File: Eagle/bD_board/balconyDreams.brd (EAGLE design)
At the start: 100 x 80 mm, 19 parts, among them IC1 7805L, U1 MKR1000, X2 MKDSN1,5/2-5,08

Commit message: add 2n7001 mosfets for relais outputs
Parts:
- added Q4: 2N7002, transistors_gaui:SOT23
- added R8: (no value), rcl:R0805
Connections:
- new net RELAIS_1_OUT: Q4.3, SV1.2
- net GND: now also Q4.2
- net RELAIS_1: now also Q4.1, R8.1; no longer SV1.2
- net VCC: now also R8.2
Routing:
- net RELAIS_1: track 29.9 -> 1.93 mm

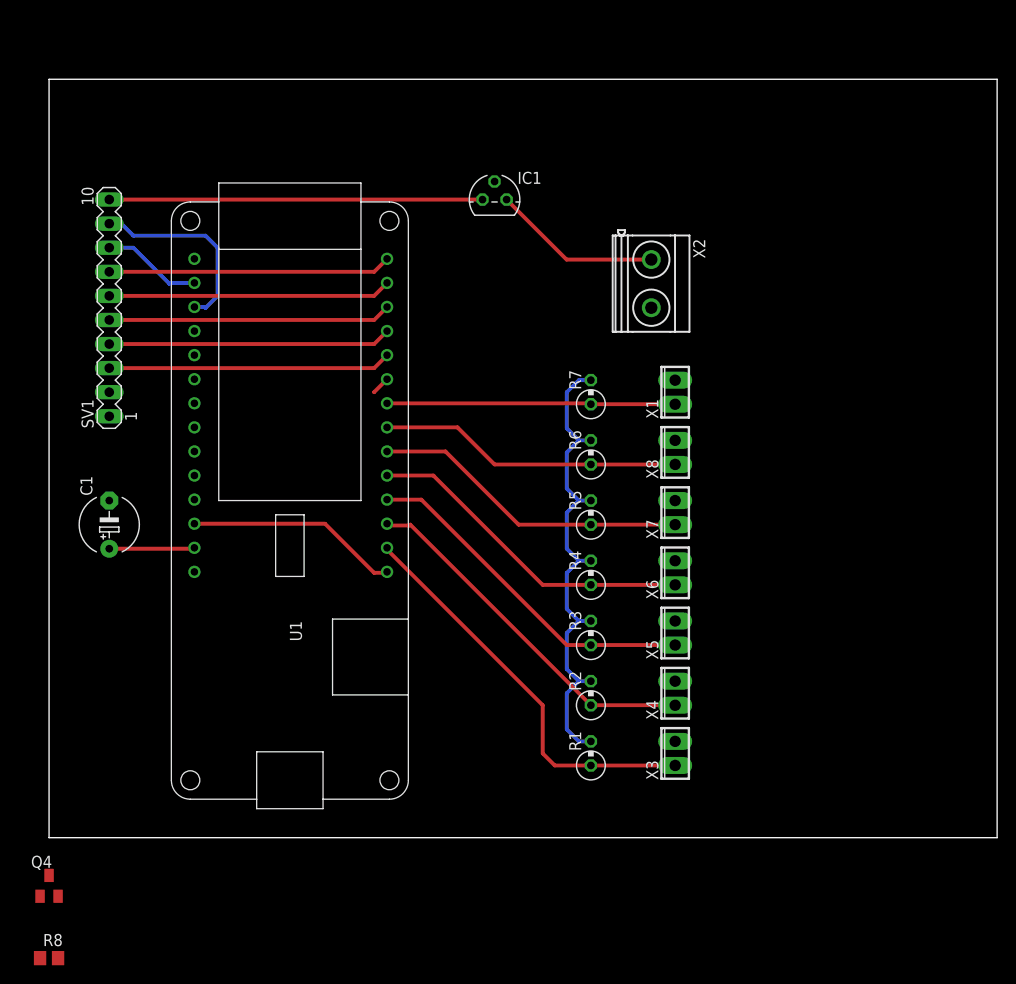
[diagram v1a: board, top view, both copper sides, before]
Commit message: add mosfets for all relais outputs
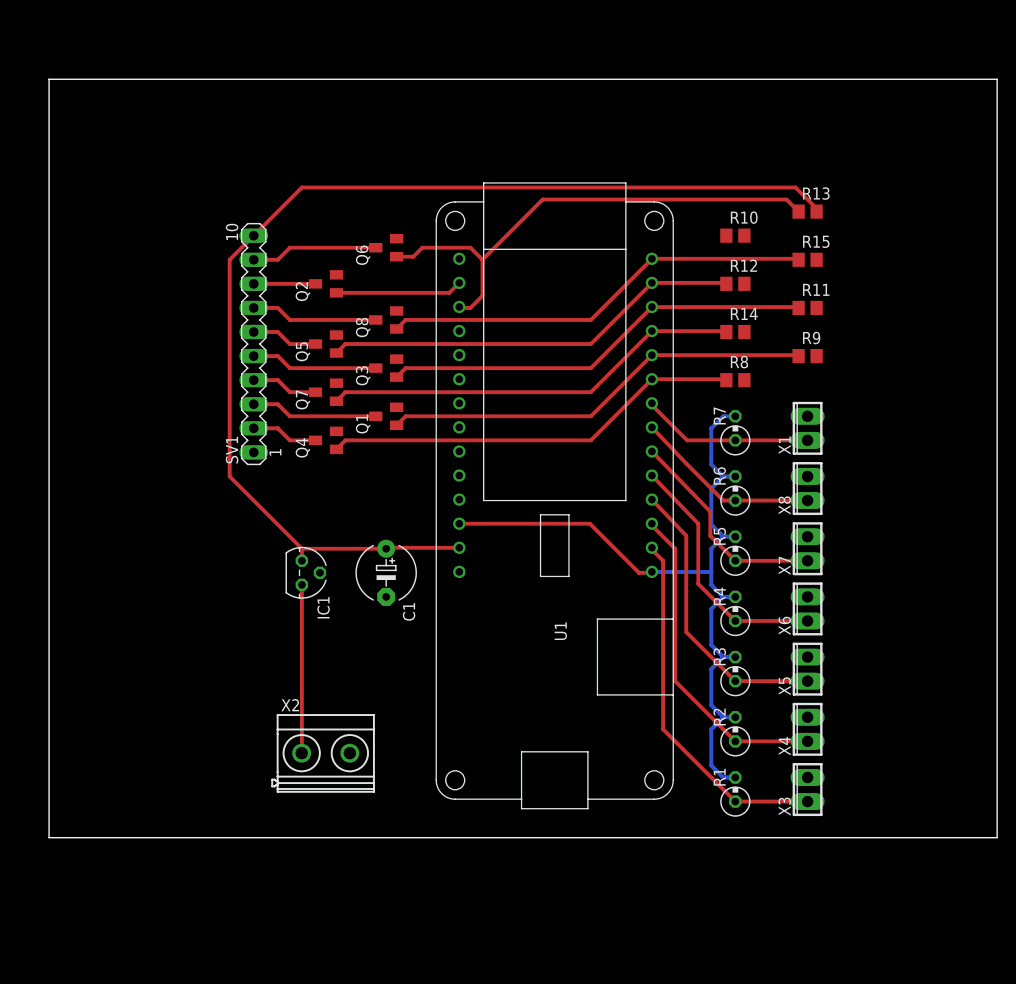
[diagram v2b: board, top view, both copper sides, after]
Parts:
- added Q1, Q2, Q3, Q5, Q6, Q7, Q8: 2N7002, transistors_gaui:SOT23
- added R10, R11, R12, R13, R14, R15, R9: (no value), rcl:R0805
- moved R8 94.6 mm to (72.4, 48.3)
- moved X2 60.2 mm to (29.2, 8.89), turned to 0 degrees
- moved Q4 55.3 mm to (29.2, 41.9), turned to 90 degrees
- moved IC1 44.3 mm to (26.7, 27.9), turned to 270 degrees
- moved C1 29.6 mm to (35.6, 27.9), turned to 270 degrees
- moved U1 27.9 mm to (53.3, 35.6)
- moved R1 15.7 mm to (72.4, 5.08)
- moved R2 15.7 mm to (72.4, 11.4)
- moved R3 15.7 mm to (72.4, 17.8)
- moved R4 15.7 mm to (72.4, 24.1)
- moved R5 15.7 mm to (72.4, 30.5)
- moved R6 15.7 mm to (72.4, 36.8)
- moved R7 15.7 mm to (72.4, 43.2)
- moved SV1 15.7 mm to (21.6, 52.1)
- moved X1 14.5 mm to (80.0, 43.2)
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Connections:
- new net RELAIS_2_OUT: Q1.3, SV1.3
- new net RELAIS_3_OUT: Q7.3, SV1.4
- new net RELAIS_4_OUT: Q3.3, SV1.5
- new net RELAIS_5_OUT: Q5.3, SV1.6
- new net RELAIS_6_OUT: Q8.3, SV1.7
- new net RELAIS_7_OUT: Q2.3, SV1.8
- new net RELAIS_8_OUT: Q6.3, SV1.9
- net GND: now also Q1.2, Q2.2, Q3.2, Q5.2, Q6.2, Q7.2, Q8.2
- net RELAIS_2: now also Q1.1, R9.1; no longer SV1.3
- net RELAIS_3: now also Q7.1, R14.1; no longer SV1.4
- net RELAIS_4: now also Q3.1, R11.1; no longer SV1.5
- net RELAIS_5: now also Q5.1, R12.1; no longer SV1.6
- net RELAIS_6: now also Q8.1, R15.1; no longer SV1.7
- net RELAIS_7: now also Q2.1, R10.1; no longer SV1.8
- net RELAIS_8: now also Q6.1, R13.1; no longer SV1.9
- net VCC: now also R10.2, R11.2, R12.2, R13.2, R14.2, R15.2, R9.2
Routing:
- net VCC: track 48.4 -> 117.9 mm
- net RELAIS_1: track 1.93 -> 44.2 mm
- net RELAIS_8: track 20.6 -> 53.3 mm
- net RELAIS_2: track 29.9 -> 45.5 mm
- net RELAIS_6: track 29.9 -> 45.5 mm
- net RELAIS_4: track 29.9 -> 45.5 mm
- net RELAIS_5: track 29.9 -> 44.2 mm
- net RELAIS_3: track 29.9 -> 44.2 mm
- net RELAIS_6_OUT: track 0.00 -> 13.4 mm
- net RELAIS_8_OUT: track 0.00 -> 13.4 mm
- net RELAIS_4_OUT: track 0.00 -> 13.4 mm
- net RELAIS_2_OUT: track 0.00 -> 13.4 mm
- net A5: track 32.0 -> 19.7 mm
- net A6: track 30.4 -> 18.2 mm
- net A4: track 33.6 -> 22.7 mm
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
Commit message: wired resistors replaced by SMD
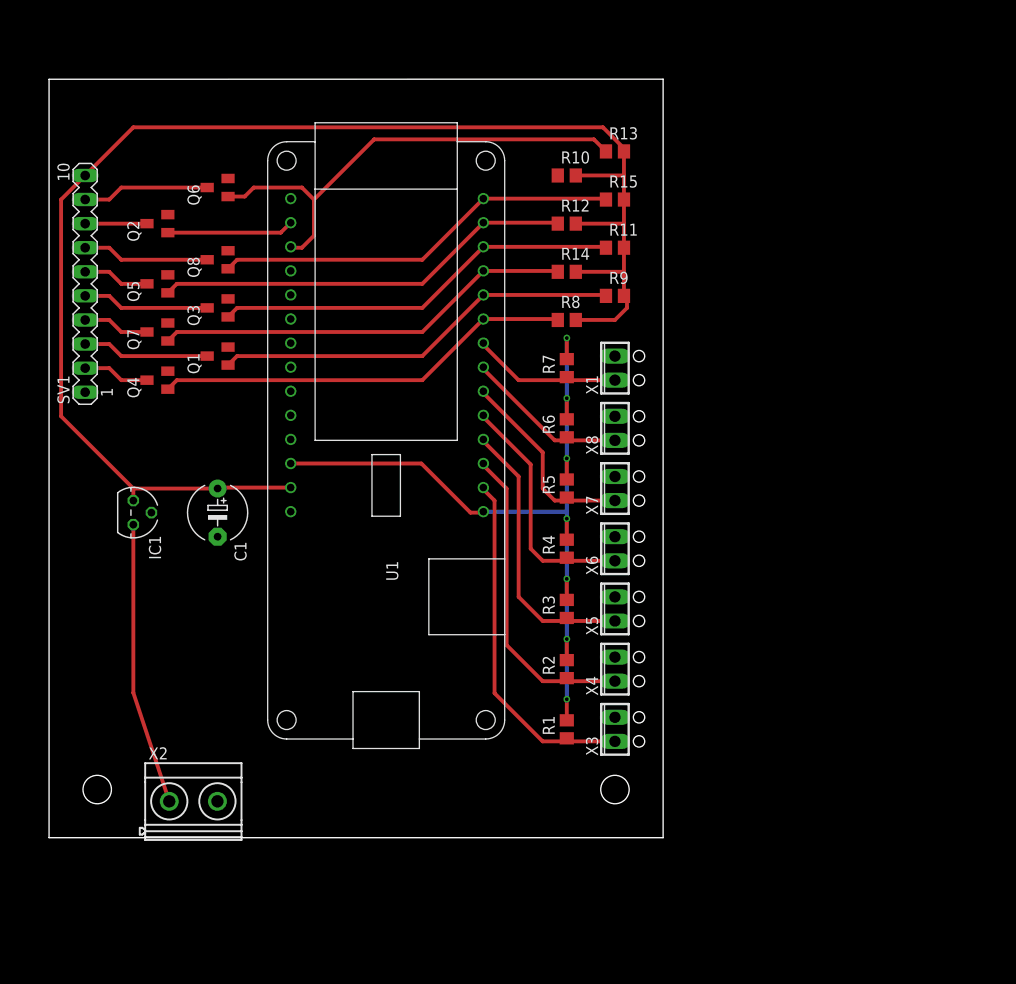
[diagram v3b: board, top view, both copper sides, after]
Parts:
- R1, R2, R3, R4, R5, R6, R7: device rcl:0309V -> rcl:R0805
- moved R15 21.3 mm to (59.7, 67.3)
- moved R9 21.3 mm to (59.7, 57.1)
- moved X1 21.3 mm to (59.7, 49.5)
- moved X3 21.3 mm to (59.7, 11.4)
- moved X4 21.3 mm to (59.7, 17.8)
- moved X6 21.3 mm to (59.7, 30.5)
- moved X8 21.3 mm to (59.7, 43.2)
- moved R11 21.3 mm to (59.7, 62.2)
- moved R13 21.3 mm to (59.7, 72.4)
- moved X5 21.3 mm to (59.7, 24.1)
- moved X7 21.3 mm to (59.7, 36.8)
- moved C1 18.9 mm to (17.8, 34.3)
- moved IC1 18.9 mm to (8.89, 34.3)
- moved Q1 18.9 mm to (17.8, 50.8)
- moved Q2 18.9 mm to (11.4, 64.8)
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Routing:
- net VCC: track 117.9 -> 153.1 mm
- net V_INPUT: track 17.8 -> 29.8 mm
- net +3V3: track 82.1 -> 85.5 mm, vias 0 -> 7
- net RELAIS_6: track 45.5 -> 43.0 mm
- net RELAIS_4: track 45.5 -> 43.0 mm
- net RELAIS_2: track 45.5 -> 43.0 mm
- net RELAIS_8: track 53.3 -> 50.8 mm
- net A6: track 18.2 -> 15.9 mm
- net A5: track 19.7 -> 17.6 mm
- net A4: track 22.7 -> 21.3 mm
- net A1: track 34.2 -> 33.4 mm
- net A0: track 38.0 -> 37.2 mm
- net A2: track 30.4 -> 29.6 mm
- net A3: track 26.6 -> 25.8 mm
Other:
- board size 100 x 80 mm -> 64.8 x 80 mm

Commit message: Lots of stuff - ready for review
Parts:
- added C2: 0.33uF, rcl:E5-6
- added D1, D2, D3, D4, D5, D6, D7: (no value), diode:SOD323-W
- added LED1, LED2, LED3: (no value), led:CHIPLED_0805
- added Q10, Q11, Q9: 2N7002, transistors_gaui:SOT23
- added R16, R18, R20: 10k, rcl:R0805
- added R17, R19, R21: 330R, rcl:R0805
- C1: value (none) -> 1uF
- IC1: value 7805L -> 7805TV; device linear:TO92 -> linear:TO220V
- R10, R11, R12, R13, R14, R15, R8, R9: value (none) -> 10k
- moved IC1 20.1 mm to (15.2, 15.2), turned to 0 degrees
- moved R11 6.35 mm to (53.3, 62.2)
- moved R13 6.35 mm to (53.3, 72.4)
- moved R15 6.35 mm to (53.3, 67.3)
- moved R9 6.35 mm to (53.3, 57.1)
- moved C1 5.12 mm to (17.1, 39.4), turned to 90 degrees
- moved R10 5.08 mm to (59.7, 69.8)
- moved R12 5.08 mm to (59.7, 64.8)
- moved R14 5.08 mm to (59.7, 59.7)
- moved R8 5.08 mm to (59.7, 54.6)
- moved X1 2.54 mm to (62.2, 49.5)
- moved X3 2.54 mm to (62.2, 11.4)
- moved X4 2.54 mm to (62.2, 17.8)
- moved X5 2.54 mm to (62.2, 24.1)
- moved X6 2.54 mm to (62.2, 30.5)
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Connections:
- new net LED1: Q9.1, R16.1, U1.18
- new net LED2: Q10.1, R18.1, U1.19
- new net LED3: Q11.1, R20.1, U1.20
- new net N$1: LED1.C, R17.1
- new net N$2: Q9.3, R17.2
- new net N$3: Q10.3, R19.2
- new net N$4: LED2.C, R19.1
- new net N$5: Q11.3, R21.2
- new net N$6: LED3.C, R21.1
- net A0: now also D1.C
- net A1: now also D2.C
- net A2: now also D3.C
- net A3: now also D4.C
- net A4: now also D5.C
- net A5: now also D6.C
- net A6: now also D7.C
- net GND: now also C2.-, D1.A, D2.A, D3.A, D4.A, D5.A, D6.A, D7.A, Q10.2, Q11.2, Q9.2, R16.2, R18.2, R20.2
- net VCC: now also IC1.3, LED1.A, LED2.A, LED3.A; no longer IC1.1
- net V_INPUT: now also C2.+, IC1.1; no longer IC1.3
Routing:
- net LED1: track 0.00 -> 56.3 mm, vias 0 -> 1
- net VCC: track 153.1 -> 201.7 mm
- net LED2: track 0.00 -> 47.4 mm, vias 0 -> 1
- net LED3: track 0.00 -> 38.0 mm, vias 0 -> 1
- net RELAIS_7: track 13.4 -> 49.4 mm, vias 0 -> 1
- net V_INPUT: track 29.8 -> 14.0 mm
- net RELAIS_8: track 50.8 -> 45.0 mm
- net RELAIS_6: track 43.0 -> 37.3 mm
- net RELAIS_2: track 43.0 -> 37.3 mm
- net RELAIS_1: track 44.2 -> 50.0 mm
- net RELAIS_3: track 44.2 -> 49.9 mm
- net RELAIS_5: track 44.2 -> 49.9 mm
- net RELAIS_4: track 43.0 -> 37.3 mm
- net A1: track 33.4 -> 37.4 mm
- net A6: track 15.9 -> 19.8 mm
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- added copper zone on layer 1, net GND
- added copper zone on layer 16, net GND
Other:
- board size 64.8 x 80 mm -> 67.3 x 80 mm
- board text added: "7-30V"
- board text added: "April 2017"
- board text added: "Balcony Dreams forever"

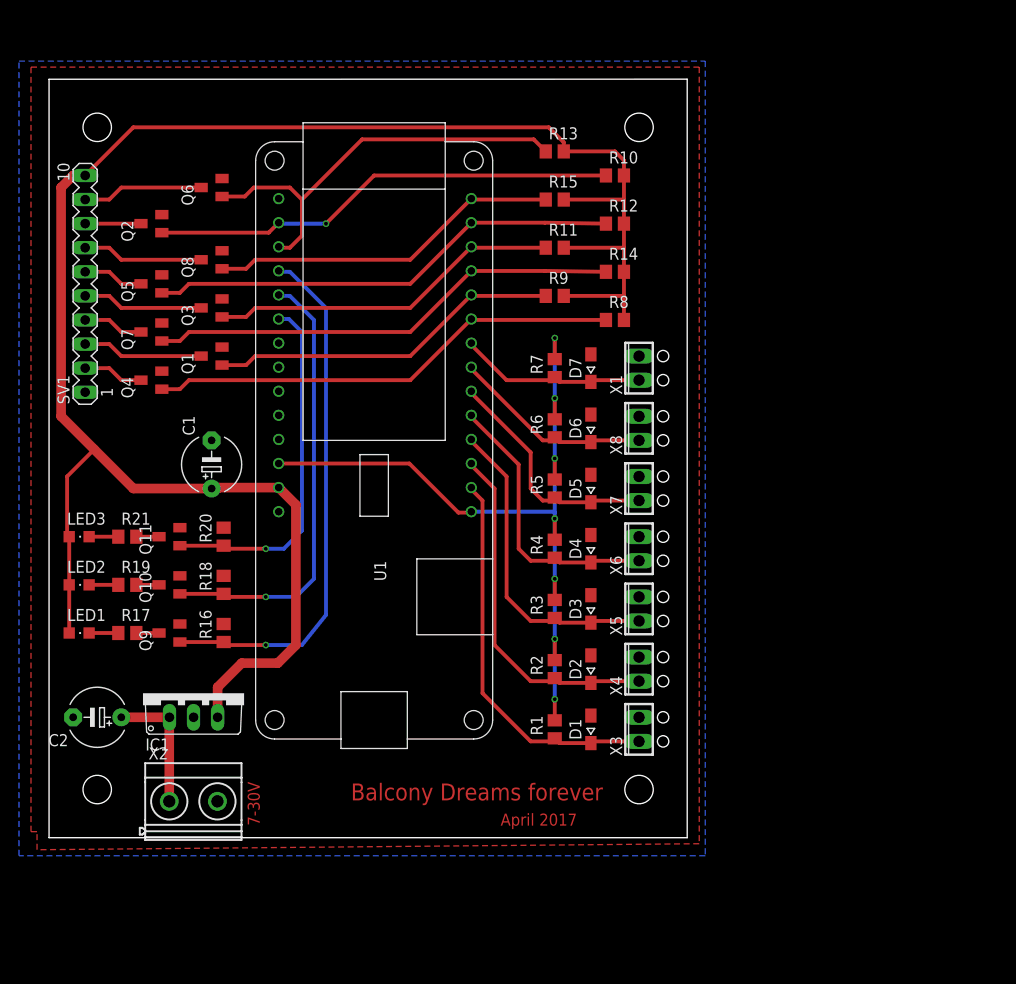
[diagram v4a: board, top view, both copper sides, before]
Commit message: add GND connectors for valves
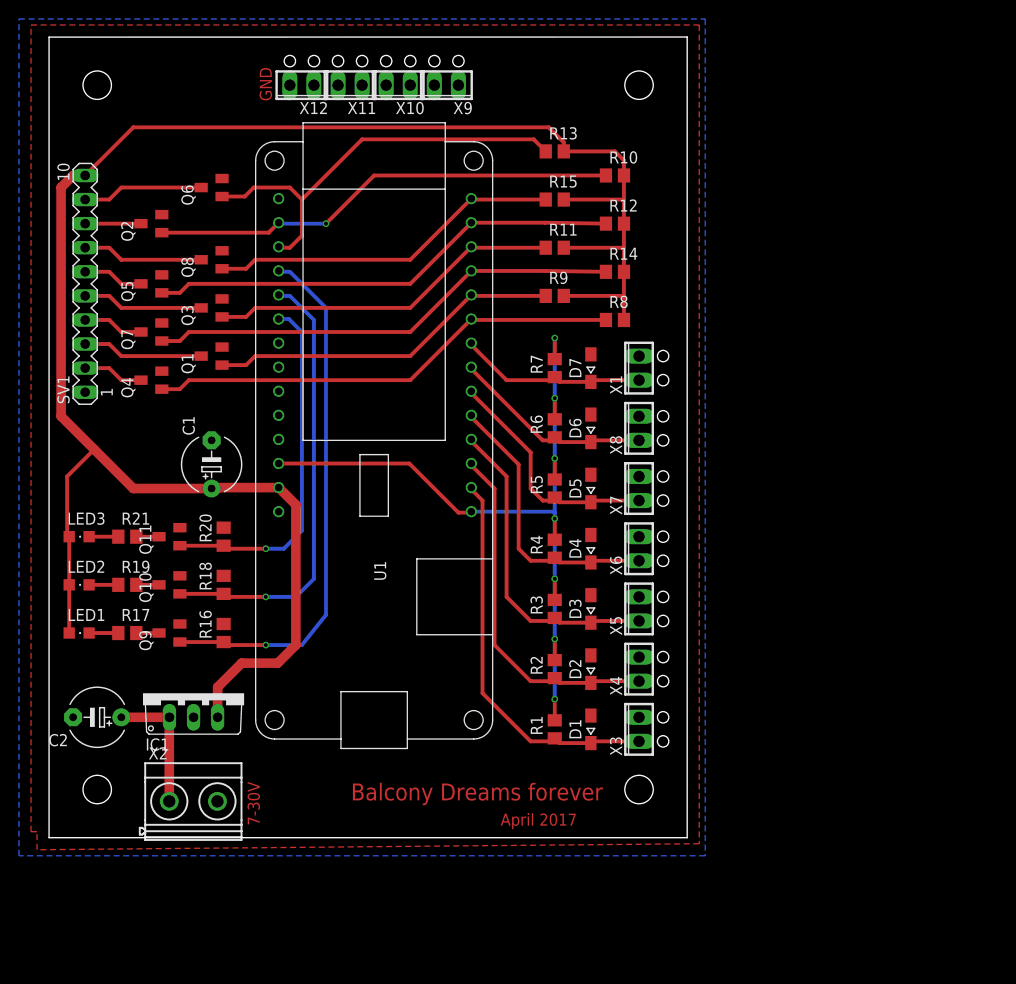
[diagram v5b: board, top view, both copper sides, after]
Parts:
- added X10, X11, X12, X9: (no value), con-phoenix-254:2POL254
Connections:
- net GND: now also X10.1, X10.2, X11.1, X11.2, X12.1, X12.2, X9.1, X9.2
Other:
- board size 67.3 x 80 mm -> 67.3 x 84.5 mm
- board text added: "GND"
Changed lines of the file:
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@@
 <plain>
 <wire x1="0" y1="0" x2="67.31" y2="0" width="0" layer="20"/>
-<wire x1="67.31" y1="0" x2="67.31" y2="80.01" width="0" layer="20"/>
-<wire x1="67.31" y1="80.01" x2="0" y2="80" width="0" layer="20"/>
-<wire x1="0" y1="80" x2="0" y2="0" width="0" layer="20"/>
+<wire x1="67.31" y1="0" x2="67.31" y2="84.455" width="0" layer="20"/>
+<wire x1="67.31" y1="84.455" x2="0" y2="84.445" width="0" layer="20"/>
+<wire x1="0" y1="84.445" x2="0" y2="0" width="0" layer="20"/>
 <hole x="64.77" y="10.16" drill="1.2"/>
 <hole x="64.77" y="12.7" drill="1.2"/>
@@
 <hole x="62.23" y="5.08" drill="3"/>
 <text x="58.42" y="5.715" size="1.778" layer="1" font="vector" ratio="12" rot="R180">Balcony Dreams forever</text>
-<hole x="5.08" y="74.93" drill="3"/>
-<hole x="62.23" y="74.93" drill="3"/>
+<hole x="5.08" y="79.375" drill="3"/>
+<hole x="62.23" y="79.375" drill="3"/>
 <text x="47.625" y="1.27" size="1.27" layer="1" font="vector" ratio="12">April 2017</text>
 <text x="22.225" y="1.27" size="1.27" layer="1" font="vector" ratio="12" rot="R90">7-30V</text>
+<hole x="43.18" y="81.915" drill="1.2"/>
+<hole x="40.64" y="81.915" drill="1.2"/>
+<hole x="38.1" y="81.915" drill="1.2"/>
+<hole x="35.56" y="81.915" drill="1.2"/>
+<hole x="33.02" y="81.915" drill="1.2"/>
+<hole x="30.48" y="81.915" drill="1.2"/>
+<hole x="27.94" y="81.915" drill="1.2"/>
+<hole x="25.4" y="81.915" drill="1.2"/>
+<text x="22.225" y="81.28" size="1.27" layer="1" font="vector" ratio="12" rot="R270">GND</text>
 </plain>
 <attributes>
@@
 <element name="LED3" library="led" package="CHIPLED_0805" value="" x="3.175" y="31.75" rot="R270"/>
 <element name="C2" library="rcl" package="E5-6" value="0.33uF" x="5.08" y="12.7" rot="R180"/>
+<element name="X9" library="con-phoenix-254" package="2POL254" value="" x="41.91" y="79.375" rot="R180">
+<attribute name="MPN" value="" x="41.91" y="79.375" size="1.27" layer="27" font="vector" ratio="12" rot="R180" display="off"/>
+<attribute name="OC_NEWARK" value="unknown" x="41.91" y="79.375" size="1.27" layer="27" font="vector" ratio="12" rot="R180" display="off"/>
+<attribute name="MF" value="" x="41.91" y="79.375" size="1.27" layer="27" font="vector" ratio="12" rot="R180" display="off"/>
+<attribute name="OC_FARNELL" value="unknown" x="41.91" y="79.375" size="1.27" layer="27" font="vector" ratio="12" rot="R180" display="off"/>
+</element>
+<element name="X10" library="con-phoenix-254" package="2POL254" value="" x="36.83" y="79.375" rot="R180">
+<attribute name="MPN" value="" x="36.83" y="79.375" size="1.27" layer="27" font="vector" ratio="12" rot="R180" display="off"/>
+<attribute name="OC_NEWARK" value="unknown" x="36.83" y="79.375" size="1.27" layer="27" font="vector" ratio="12" rot="R180" display="off"/>
+<attribute name="MF" value="" x="36.83" y="79.375" size="1.27" layer="27" font="vector" ratio="12" rot="R180" display="off"/>
+<attribute name="OC_FARNELL" value="unknown" x="36.83" y="79.375" size="1.27" layer="27" font="vector" ratio="12" rot="R180" display="off"/>
+</element>
+<element name="X11" library="con-phoenix-254" package="2POL254" value="" x="31.75" y="79.375" rot="R180">
+<attribute name="MPN" value="" x="31.75" y="79.375" size="1.27" layer="27" font="vector" ratio="12" rot="R180" display="off"/>
+<attribute name="OC_NEWARK" value="unknown" x="31.75" y="79.375" size="1.27" layer="27" font="vector" ratio="12" rot="R180" display="off"/>
+<attribute name="MF" value="" x="31.75" y="79.375" size="1.27" layer="27" font="vector" ratio="12" rot="R180" display="off"/>
+<attribute name="OC_FARNELL" value="unknown" x="31.75" y="79.375" size="1.27" layer="27" font="vector" ratio="12" rot="R180" display="off"/>
+</element>
+<element name="X12" library="con-phoenix-254" package="2POL254" value="" x="26.67" y="79.375" rot="R180">
+<attribute name="MPN" value="" x="26.67" y="79.375" size="1.27" layer="27" font="vector" ratio="12" rot="R180" display="off"/>
+<attribute name="OC_NEWARK" value="unknown" x="26.67" y="79.375" size="1.27" layer="27" font="vector" ratio="12" rot="R180" display="off"/>
+<attribute name="MF" value="" x="26.67" y="79.375" size="1.27" layer="27" font="vector" ratio="12" rot="R180" display="off"/>
+<attribute name="OC_FARNELL" value="unknown" x="26.67" y="79.375" size="1.27" layer="27" font="vector" ratio="12" rot="R180" display="off"/>
+</element>
 </elements>
 <signals>
@@
 <contactref element="Q8" pad="2"/>
 <polygon width="0.4064" layer="16">
-<vertex x="-3.175" y="81.915"/>
-<vertex x="69.215" y="81.915"/>
+<vertex x="-3.175" y="86.36"/>
+<vertex x="69.215" y="86.36"/>
 <vertex x="69.215" y="-1.905"/>
 <vertex x="-3.175" y="-1.905"/>
 </polygon>
 <polygon width="0.4064" layer="1">
-<vertex x="-1.905" y="81.28"/>
-<vertex x="68.58" y="81.28"/>
+<vertex x="-1.905" y="85.725"/>
+<vertex x="68.58" y="85.725"/>
 <vertex x="68.58" y="-0.635"/>
 <vertex x="-1.27" y="-1.27"/>
@@
 <contactref element="R20" pad="2"/>
 <contactref element="C2" pad="-"/>
+<contactref element="X12" pad="2"/>
+<contactref element="X12" pad="1"/>
+<contactref element="X11" pad="2"/>
+<contactref element="X11" pad="1"/>
+<contactref element="X10" pad="2"/>
+<contactref element="X10" pad="1"/>
+<contactref element="X9" pad="2"/>
+<contactref element="X9" pad="1"/>
 </signal>
 <signal name="VCC">
